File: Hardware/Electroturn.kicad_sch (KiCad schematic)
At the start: 13 parts

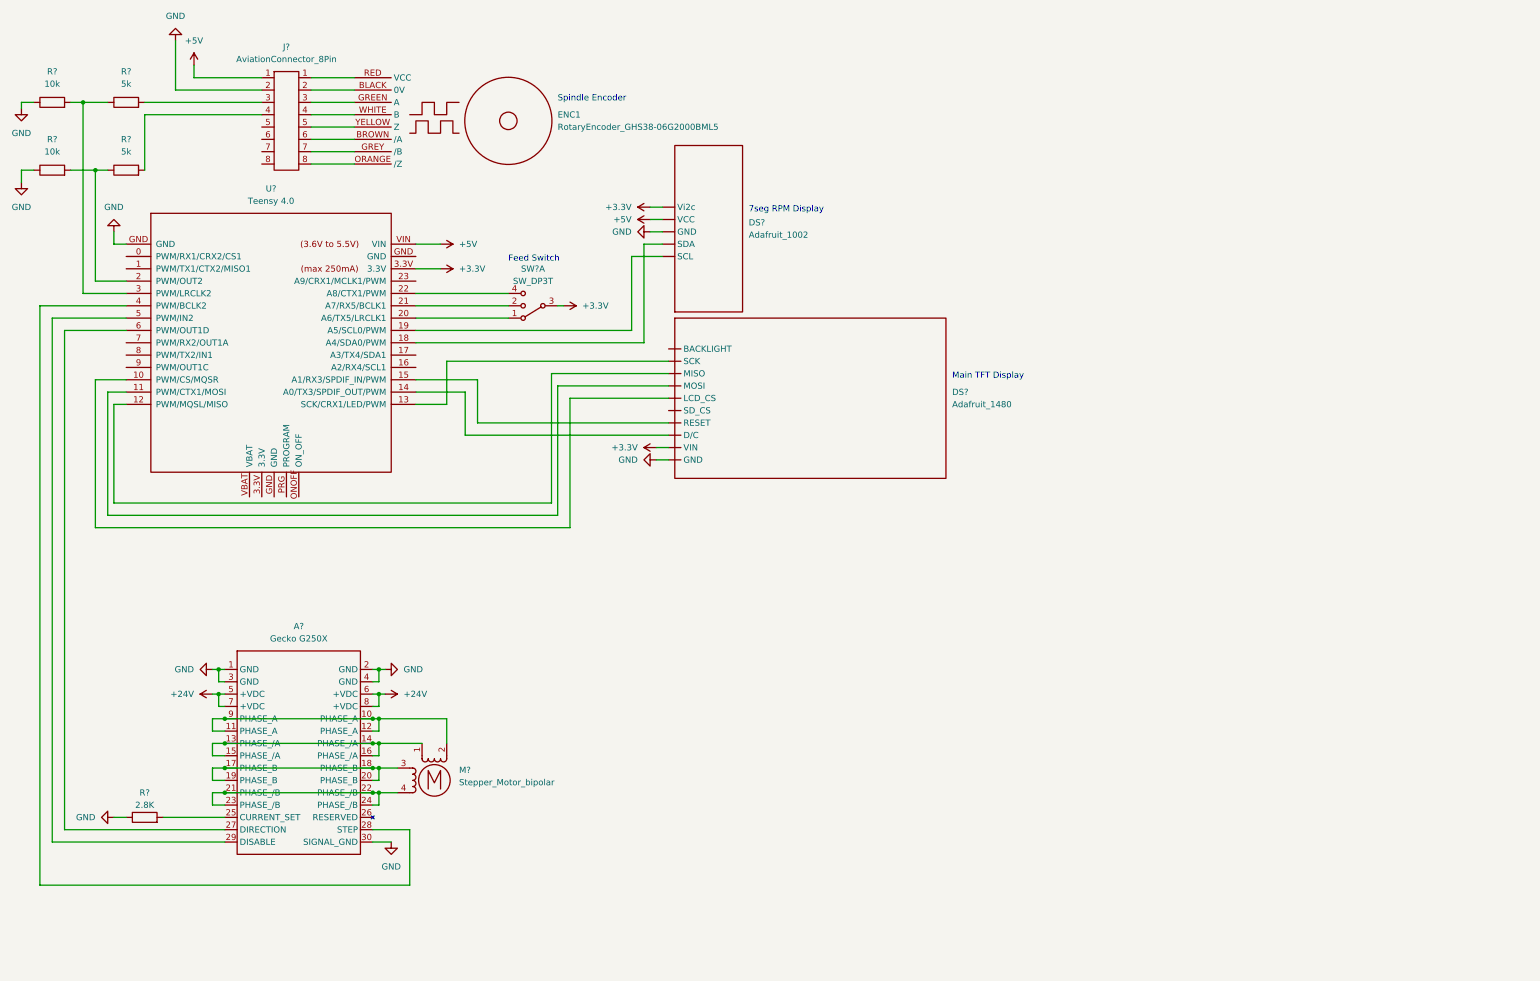
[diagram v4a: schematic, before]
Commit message: New branch for pcb work
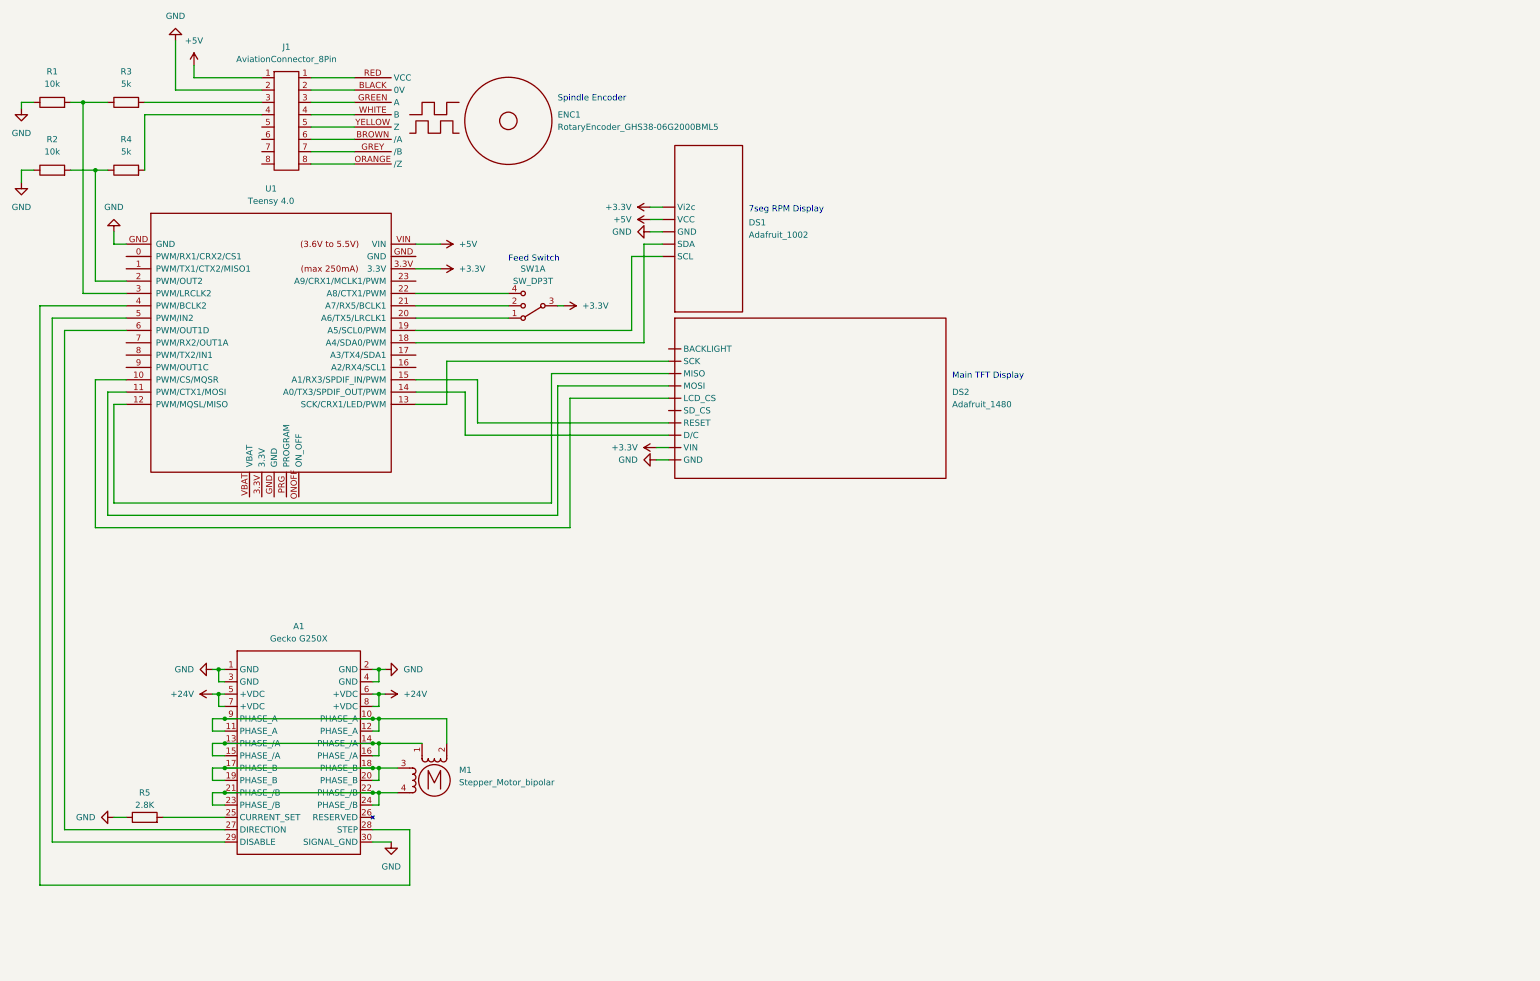
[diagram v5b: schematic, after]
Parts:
- U1: renamed from U?; footprint (none) -> teensy:Teensy40
- gave numbers to parts that had none: 11

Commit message: Adding 3D models, improving footprints for Teensy and Gecko, adding screw terminals to schematic
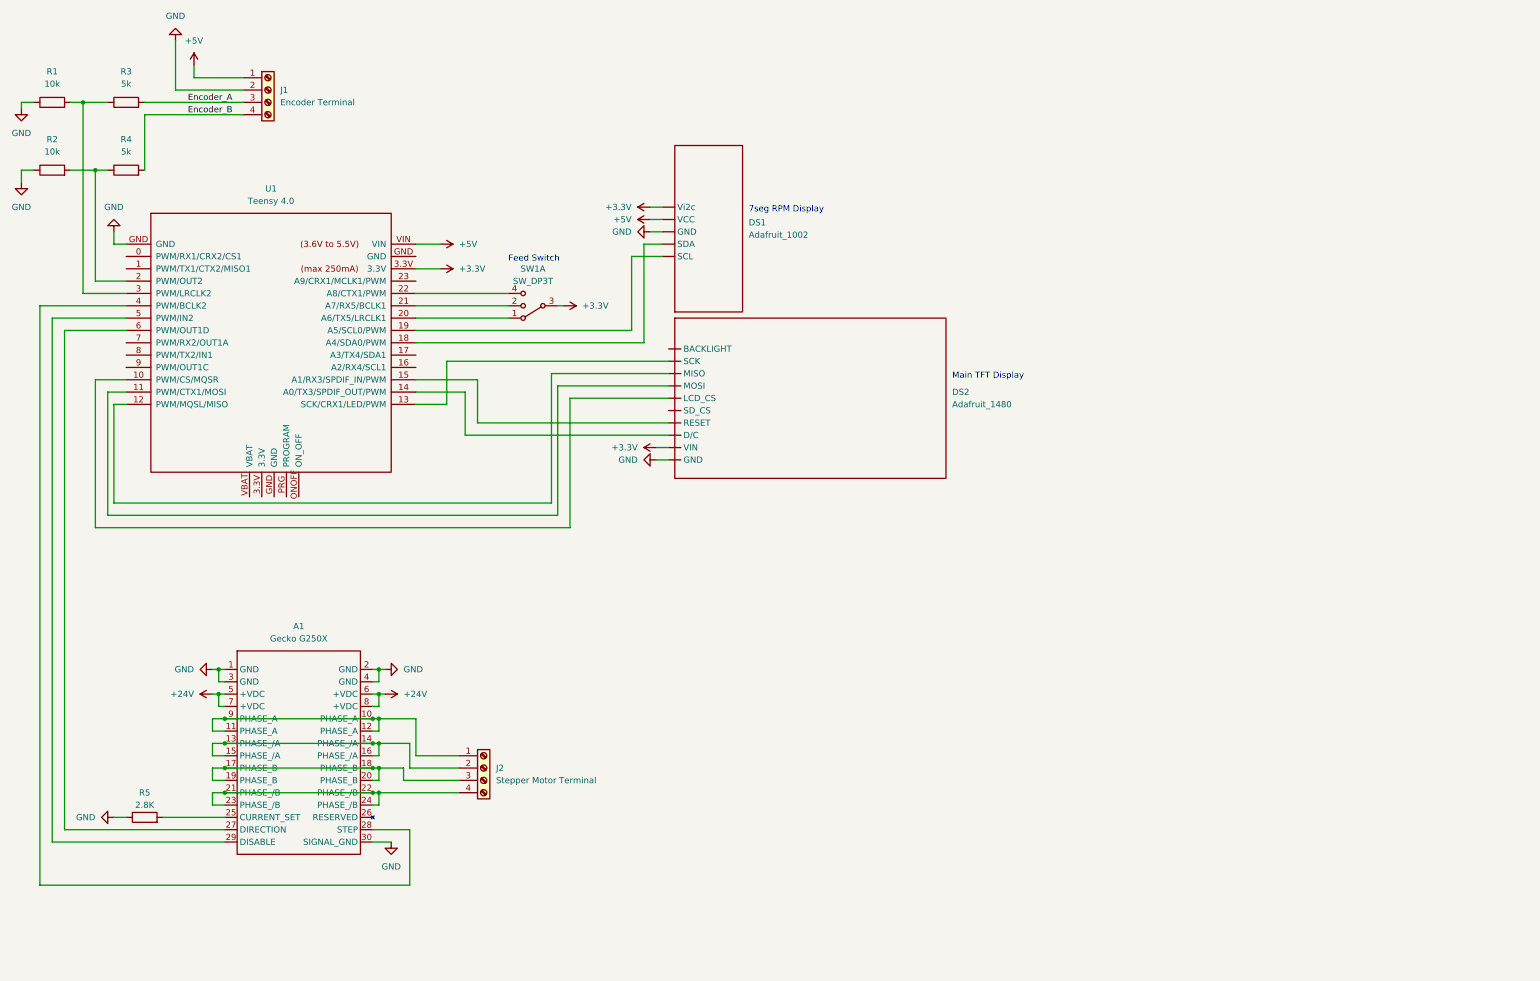
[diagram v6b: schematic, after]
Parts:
- removed ENC1: RotaryEncoder_GHS38-06G2000BML5, symbol Electroturn_Parts:RotaryEncoder_GHS38-06G2000BML5
- removed J1: AviationConnector_8Pin, symbol Electroturn_Parts:AviationConnector_8Pin
- removed M1: Stepper_Motor_bipolar, symbol Motor:Stepper_Motor_bipolar
- added J1: Encoder Terminal, Electroturn_Parts:ScrewTerminal4_OSTVN04A150, symbol Connector:Screw_Terminal_01x04
- added J2: Stepper Motor Terminal, Electroturn_Parts:ScrewTerminal4_OSTVN04A150, symbol Connector:Screw_Terminal_01x04
- A1: footprint (none) -> Electroturn_Parts:GeckoG250XR2_WithHeatsink
- R1, R2, R3, R4, R5: footprint (none) -> Resistor_THT:R_Axial_DIN0411_L9.9mm_D3.6mm_P12.70mm_Horizontal
- U1: footprint teensy:Teensy40 -> Electroturn_Parts:Teensy40_OnFemaleHeaders
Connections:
- net +5V: now also J1.1 (Pin_1)
- net GND: now also J1.2 (Pin_2)
- net at A1.10 (PHASE_A), A1.11 (PHASE_A), A1.12 (PHASE_A)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: now also J2.1 (Pin_1)
- net at A1.13 (PHASE_/A), A1.14 (PHASE_/A), A1.15 (PHASE_/A)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: now also J2.2 (Pin_2)
- net at A1.17 (PHASE_B), A1.18 (PHASE_B), A1.19 (PHASE_B)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: now also J2.3 (Pin_3)
- net at A1.21 (PHASE_/B), A1.22 (PHASE_/B), A1.23 (PHASE_/B)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: now also J2.4 (Pin_4)
- net Encoder_A: now reaches R3.2
- net Encoder_A: now also J1.3 (Pin_3)
- net Encoder_B: now reaches R4.2
- net Encoder_B: now also J1.4 (Pin_4)
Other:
- note removed: "Spindle Encoder"

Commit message: Adding MCP23017 (i2c IO chip) to schematic, other housekeeping
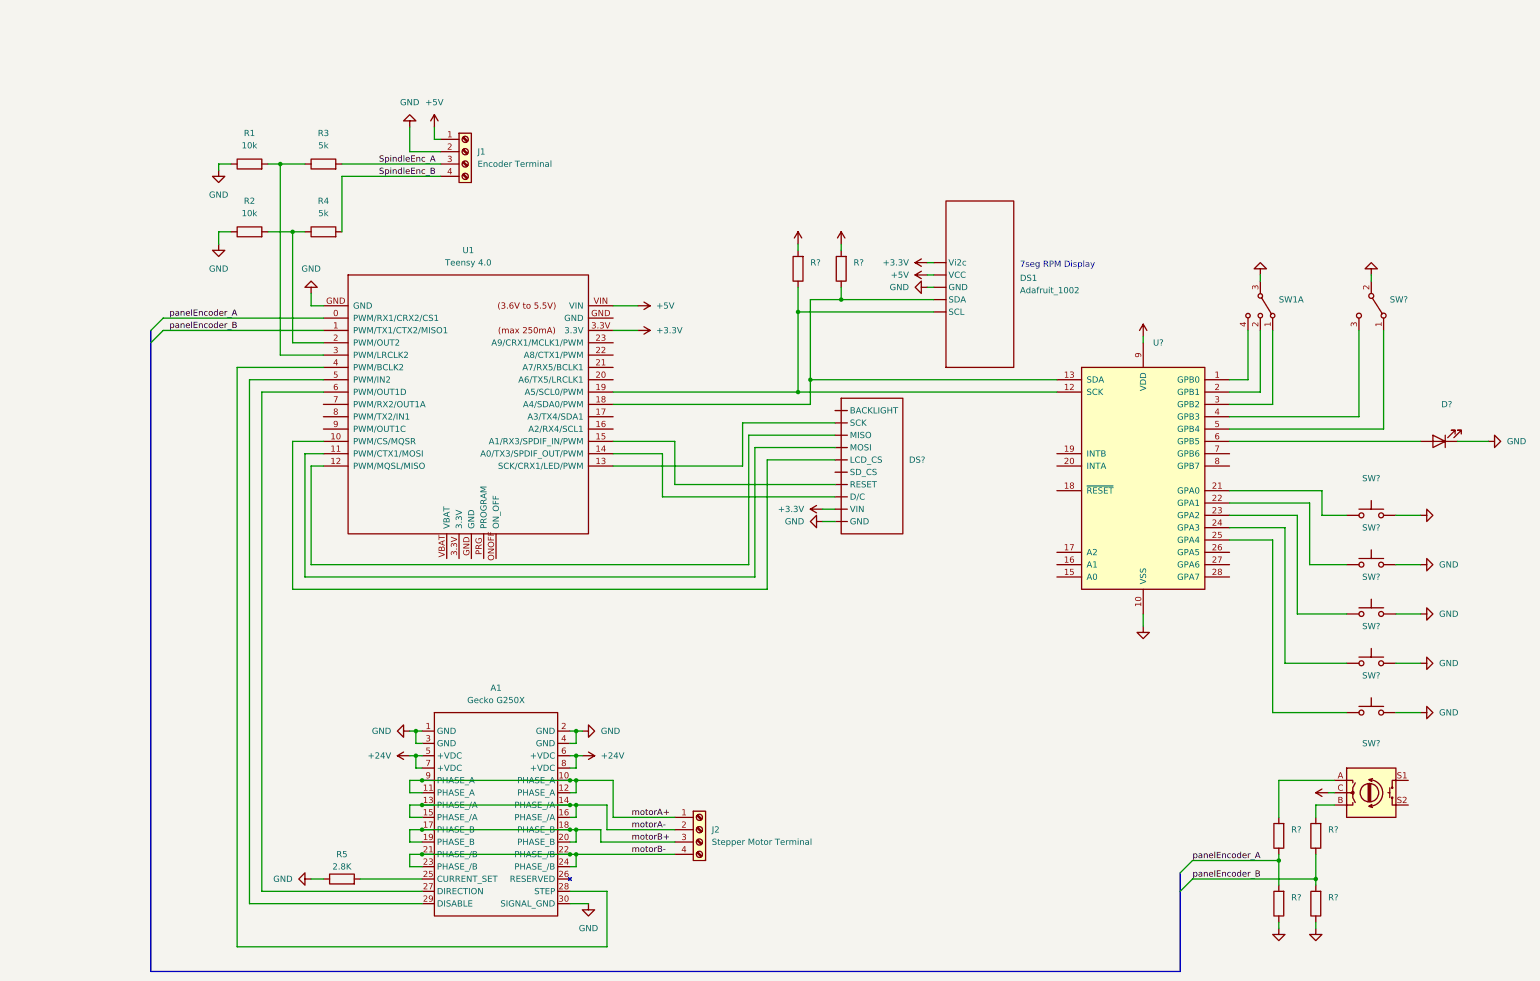
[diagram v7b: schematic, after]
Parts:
- removed DS2: Adafruit_1480, symbol MCU_Module:Adafruit_1480
- added D?: (no value), symbol Device:LED
- added DS?: (no value), symbol Electroturn_Parts:Adafruit_1480_2.2inTFT
- added R? (x6): (no value), symbol Device:R
- added SW? (x5): (no value), symbol Switch:SW_Push
- added SW?: (no value), symbol Switch:SW_SPDT
- added SW?: (no value), symbol Device:RotaryEncoder_Switch
- added U?: (no value), symbol Interface_Expansion:MCP23017_SP
- SW1: value SW_DP3T -> (none)
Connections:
- net +3V3: now also DS?. (VIN), R?.2, R?.2, U?.9 (VDD); no longer SW1.3
- net +5V: now also SW?.C
- net GND: now also SW1.3, D?.1 (K), DS?. (VIN), R?.1, R?.1, SW?.2, SW?.2, SW?.2, SW?.2, SW?.2, SW?.2 (B), U?.10 (VSS)
- net motorA+: now reaches A1.10 (PHASE_A), A1.11 (PHASE_A), A1.12 (PHASE_A), A1.9 (PHASE_A), J2.1 (Pin_1)
- net motorA-: now reaches A1.13 (PHASE_/A), A1.14 (PHASE_/A), A1.15 (PHASE_/A), A1.16 (PHASE_/A), J2.2 (Pin_2)
- net motorB+: now reaches A1.17 (PHASE_B), A1.18 (PHASE_B), A1.19 (PHASE_B), A1.20 (PHASE_B), J2.3 (Pin_3)
- net motorB-: now reaches A1.21 (PHASE_/B), A1.22 (PHASE_/B), A1.23 (PHASE_/B), A1.24 (PHASE_/B), J2.4 (Pin_4)
- net panelEncoder_A: now reaches U1.0 (PWM/RX1/CRX2/CS1)
- net panelEncoder_A: now also R?.1, R?.2
- net panelEncoder_B: now reaches U1.1 (PWM/TX1/CTX2/MISO1)
- net panelEncoder_B: now also R?.1, R?.2
- net at U1.10 (PWM/CS/MQSR): now also DS?. (VIN)
- net at U1.11 (PWM/CTX1/MOSI): now also DS?. (VIN)
- net at U1.12 (PWM/MQSL/MISO): now also DS?. (VIN)
- net at U1.13 (SCK/CRX1/LED/PWM): now also DS?. (VIN)
- net at U1.14 (A0/TX3/SPDIF_OUT/PWM): now also DS?. (VIN)
- net at U1.15 (A1/RX3/SPDIF_IN/PWM): now also DS?. (VIN)
- net at DS1. (Vi2c), U1.18 (A4/SDA0/PWM): now also R?.1, U?.13 (SDA)
- net at DS1. (Vi2c), U1.19 (A5/SCL0/PWM): now also R?.1, U?.12 (SCK)
- net at U1.20 (A6/TX5/LRCLK1): no longer SW1.1
- net at U1.21 (A7/RX5/BCLK1): no longer SW1.2
- net at U1.22 (A8/CTX1/PWM): no longer SW1.4
- net Encoder_A renamed SpindleEnc_A
- net Encoder_B renamed SpindleEnc_B
- new net: SW?.1, U?.21 (GPA0)
- new net: R?.2, SW?.A
- new net: SW?.1, U?.23 (GPA2)
- new net: SW?.1, U?.22 (GPA1)
- new net: SW?.1, U?.24 (GPA3)
- new net: SW?.1 (A), U?.5 (GPB4)
- new net: SW?.3 (C), U?.4 (GPB3)
- new net: R?.2, SW?.B
- new net: SW1.4, U?.1 (GPB0)
- new net: SW1.2, U?.2 (GPB1)
- new net: SW?.1, U?.25 (GPA4)
- new net: SW1.1, U?.3 (GPB2)
- new net: D?.2 (A), U?.6 (GPB5)
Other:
- note removed: "Feed Switch"
- note removed: "Main TFT Display"
- moved on the sheet: A1, DS1, J1, J2, R1, R2, R3, R4, R5, SW1A, U1

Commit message: Consolidating most things into buses on schematic
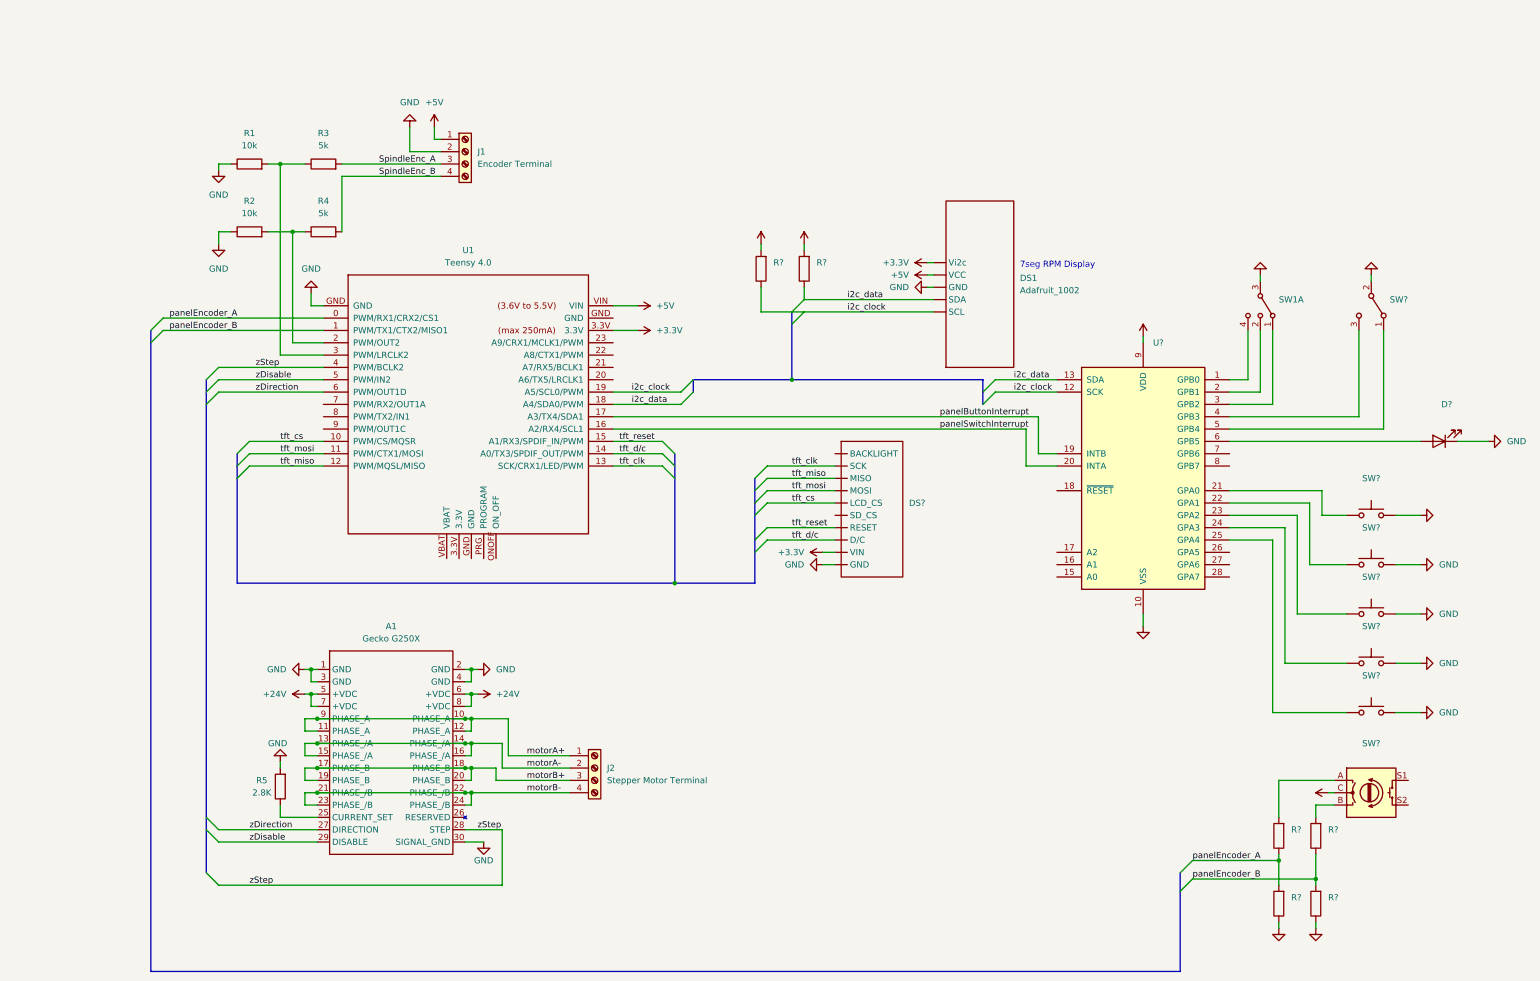
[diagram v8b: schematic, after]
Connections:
- net GND: now also R5.2; no longer R5.1
- net at A1.25 (CURRENT_SET): now also R5.1; no longer R5.2
- net zDirection: now reaches A1.27 (DIRECTION), U1.6 (PWM/OUT1D)
- net zStep: now reaches A1.28 (STEP), U1.4 (PWM/BCLK2)
- net zDisable: now reaches A1.29 (DISABLE), U1.5 (PWM/IN2)
- net tft_cs: now reaches DS?. (VIN), U1.10 (PWM/CS/MQSR)
- net tft_mosi: now reaches DS?. (VIN), U1.11 (PWM/CTX1/MOSI)
- net tft_miso: now reaches DS?. (VIN), U1.12 (PWM/MQSL/MISO)
- net tft_clk: now reaches DS?. (VIN), U1.13 (SCK/CRX1/LED/PWM)
- net tft_d/c: now reaches DS?. (VIN), U1.14 (A0/TX3/SPDIF_OUT/PWM)
- net tft_reset: now reaches DS?. (VIN), U1.15 (A1/RX3/SPDIF_IN/PWM)
- net panelSwitchInterrupt: now reaches U1.16 (A2/RX4/SCL1)
- net panelSwitchInterrupt: now also U?.20 (INTA)
- net panelButtonInterrupt: now reaches U1.17 (A3/TX4/SDA1)
- net panelButtonInterrupt: now also U?.19 (INTB)
- net i2c_data: now reaches DS1. (Vi2c), R?.1, U1.18 (A4/SDA0/PWM), U?.13 (SDA)
- net i2c_clock: now reaches DS1. (Vi2c), R?.1, U1.19 (A5/SCL0/PWM), U?.12 (SCK)
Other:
- moved on the sheet: A1, DS?, J2, R5, R?
